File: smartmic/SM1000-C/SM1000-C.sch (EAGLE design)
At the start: 193 parts, among them CN1 HDR100-3, CN10 MJ-3523-SMT, CN11 HDR100-3, CN12 HRS-DF11-16DS, CN2 MOLEX-MINI-B-SMT, CN3 RASM722PX, CN4 RJ-45, CN5 MJ-3523-SMT, CN6 SJ-3524-SMT, CN7 MJ-3523-SMT, CN8 SJ-3524-SMT, CN9 MJ-3523-SMT, J1 JMP-2PIN, J3 JMP-2PIN, J4 JMP-2PIN, P1 TPAD50, P10 TPAD50, P11 TPAD50, P12 TPAD50, P13 TPAD50, P14 TPAD50, P15 TPAD50, P16 TPAD50, P17 TPAD50, P18 TPAD50, P19 TPAD50, P2 TPAD50, P20 TPAD50, P3 TPAD50, P4 TPAD50, P5 TPAD50, P6 TPAD50, P7 TPAD50, P8 TPAD50, P9 TPAD50, SW1 SW-BOURNS-7914S, SW2 SW-BOURNS-7914S, SW3 DPDT, SW4 SW-BOURNS-7914S, SW5 SW-BOURNS-7914J, T1 SM-LP-5001, T2 SM-LP-5001, U1 STM32F405, U2 LD3985M33R, U3 STMPS2141, U4 EMIF02-USB03F2, U5 TPS54329E, U6 LMV341, U7 LMV341, U8 LM386M-1, U9 LMV341

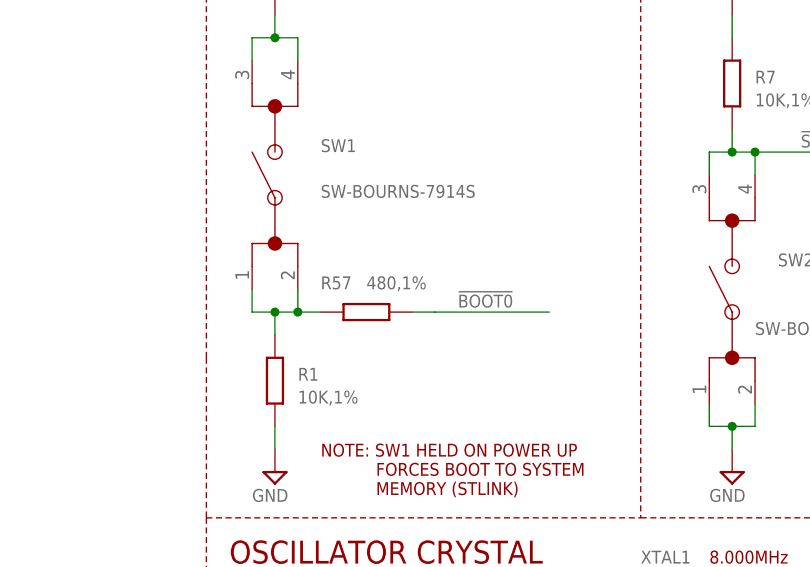
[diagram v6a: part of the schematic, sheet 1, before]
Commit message: Update 490 OHM -> 470 OHM Print both pages of schematics to PDF. RGB 10/07/14
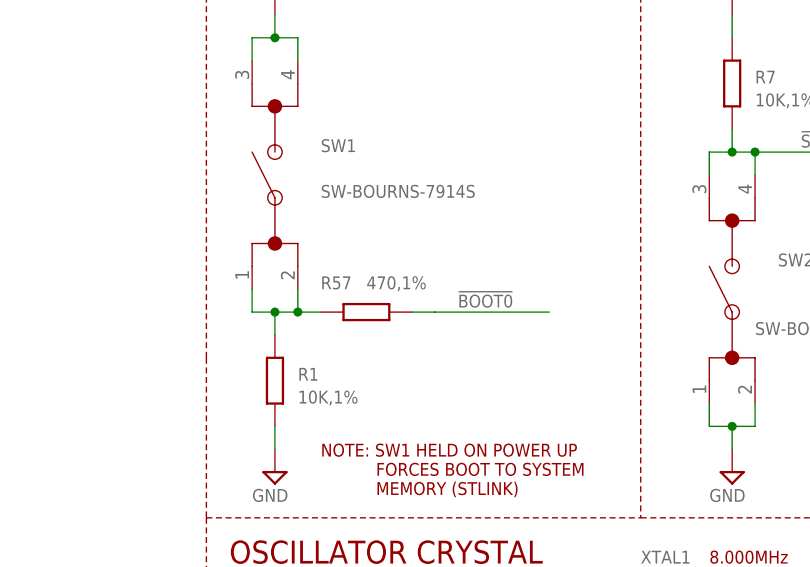
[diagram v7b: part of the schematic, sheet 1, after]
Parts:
- R57: value 480,1% -> 470,1%
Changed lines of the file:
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@@
 <part name="U$20" library="A-SUPPLY2" deviceset="GND" device=""/>
 <part name="R56" library="AA-ipc-7351-resistor" deviceset="RESISTOR_" device="0603" value="2.2K,1%"/>
-<part name="R57" library="AA-ipc-7351-resistor" deviceset="RESISTOR_" device="0603" value="480,1%"/>
+<part name="R57" library="AA-ipc-7351-resistor" deviceset="RESISTOR_" device="0603" value="470,1%"/>
 <part name="FB7" library="_RoweTel" deviceset="FB0805" device=""/>
 <part name="R58" library="AA-ipc-7351-resistor" deviceset="RESISTOR_" device="0603" value="2.2K,1%"/>

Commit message: Recovery from Eagle ERC problem RGB
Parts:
- removed L2: 4.2uH, _RoweTel:SRR5028
- added C70: 22uF,25V,1210, ipc-7351-capacitor:CAPACITOR_1210
- added L1: 4.2uH, _RoweTel:SRR5028
- C25: value 22uF,25V,6032-28,Tant -> 22uF,25V,1210; device AA-ipc-7351-capacitor:POLARISED_C_CASE -> ipc-7351-capacitor:CAPACITOR_1210
- C27: value 20pF,50V -> 20pF,16V
- C28, C29: value 10uF,25V,3528,Tant -> 10uF,25V,1206; device AA-ipc-7351-capacitor:POLARISED_B_CASE -> ipc-7351-capacitor:CAPACITOR_1206
- C40: value 47nF,25V -> 100nF,25V
- C54: value 1nF,16V -> 1nF,25V
- CN12: value HRS-DF11-16DS -> DF11-16DS
- CN3: device _RoweTel:RASM722PX -> _RoweTel:RASM712PX
- CN6, CN8: value SJ-3524-SMT -> SJ-3524
- R18, R21: device _RoweTel:RES0805 -> AA-ipc-7351-resistor:RESISTOR_0603
- SW1: device SM1000:SW-BOURNS-7914S -> SM1000-2L-70x90:SW-BOURNS-7914S
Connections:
- net !CPTT! renamed !CPPT!
- net N$15 renamed +VEXT
- removed net AVSS: C55.2, C56.2
- removed net BOOT0: U1A.PD7
- removed net N$26 (its old number): J3.1, R32.1
- removed net N$32 (its old number): C54.2, R29.1, R42.1, U9.OUT
- removed net N$67: C51.1, CN10.2, R37.1, R56.1
- removed net N$69: C32.+, C62.1, R32.2, R58.1
- new net N$11: R55.1, U1A.PA4
- new net N$15: C51.1, CN10.2, R37.2, R56.1
- new net N$27: C54.2, R29.2, R42.3, U9.OUT
- new net N$45: C32.+, C62.1, R32.1, R58.2
- new net N$81: R47.3, R49.2
- net !BOOT0!: now also U1A.PD7
- net +5V: now also C28.1, C29.1, L1.2; no longer C28.+, C29.+, L2.2
- net +VIN: now also C25.1, C70.1; no longer C25.+
- net AIN2: no longer P4.1, R29.2
- net APTT: now also CN12.14; no longer CN12.6
- net DAC1_OUT: now also R55.2; no longer R55.1
- net DAC2_OUT: now also R22.1, R54.2; no longer R22.2, R54.1
- net GND: now also C25.2, C28.2, C29.2, C55.2, C56.2, C58.1, C70.2, R22.2; no longer C25.-, C28.-, C29.-, C58.2, R22.1
- net MIC: now also CN12.15; no longer CN12.7
- net N$13: now also R54.1, U1A.PA5; no longer R47.1, R49.2
- net N$25: now also R58.1; no longer R58.2
- net N$29: now also J3.1, R32.2; no longer R55.2, U1A.PA4
- net N$36: now also P4.1, R29.1; no longer R54.2, U1A.PA5
- net N$41: now also R42.1; no longer R42.3
- net N$46: now also C58.2; no longer C58.1
- net N$51: now also CN12.8; no longer CN12.16
- net N$52: now also CN12.7; no longer CN12.15
- net N$53: now also CN12.6; no longer CN12.14
- net N$54: now also CN12.5; no longer CN12.13
- net N$55: now also CN12.4; no longer CN12.12
- net N$56: now also CN12.3; no longer CN12.11
- net N$57: now also CN12.2; no longer CN12.10
- net N$58: now also CN12.1; no longer CN12.9
- net N$82: now also R47.1; no longer R47.3
- net RF_MIC: now also CN12.11, CN12.12; no longer CN12.3, CN12.4
- net RF_PTT: now also CN12.13; no longer CN12.5
- net RF_SPKR: now also CN12.10, CN12.9; no longer CN12.1, CN12.2
- net SPKR: now also CN12.16; no longer CN12.8
- net SW: now also L1.1; no longer L2.1
- net VDD: now also R37.1; no longer R37.2
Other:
- note added: "10/13/14"
- note added: "Release For Production"
- note added: "Release for Production"
- note added: "SPEAKER AMP"
- note removed: "1. Enlarge pads on R46 POT"
- note removed: "2. AVDD has no source."
- note removed: "3. Check polarity & source of LMV341 pin 5."
- note removed: "4. Reposition 3.5mm jacks for 11.3mm plug spacing."
- note removed: "DNL"
- note removed: "FB5"
- note removed: "TODO:"
- moved on the sheet: C15, C22, C23, C26, C27, C31, C35, C36, C37, C38, C39, C40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
